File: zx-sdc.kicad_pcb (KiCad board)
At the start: 2 copper layers, 80 x 125.7 mm, 67 parts, among them J1 SD_Card, J2 Micro_SD_Card_Det2, J4 Conn_01x03_Pin, Q1 2N7000, Q2 BC557, U10 74LS125, U11 74LS595, U12 74LS30, U13 74LS138, U3 AMS1117-3.3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

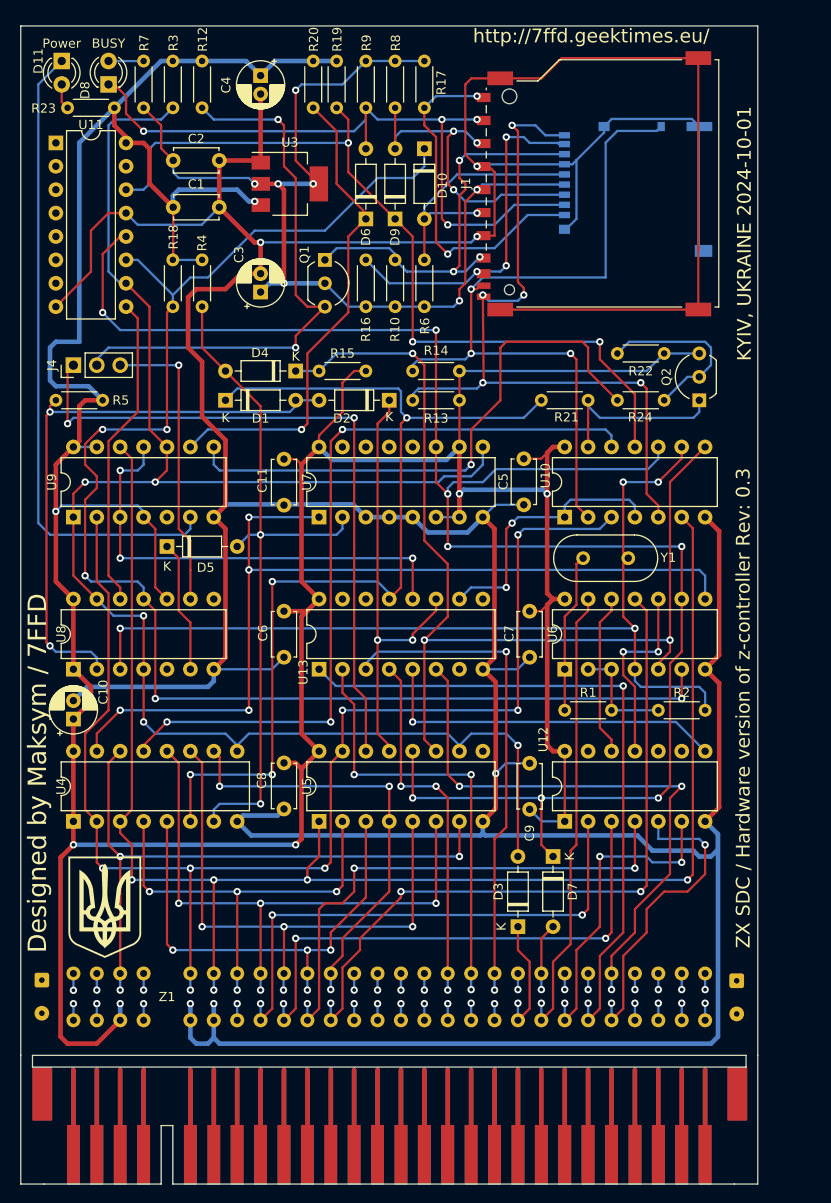
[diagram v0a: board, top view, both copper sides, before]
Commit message: fixed and annotated SD/TEST jumpers
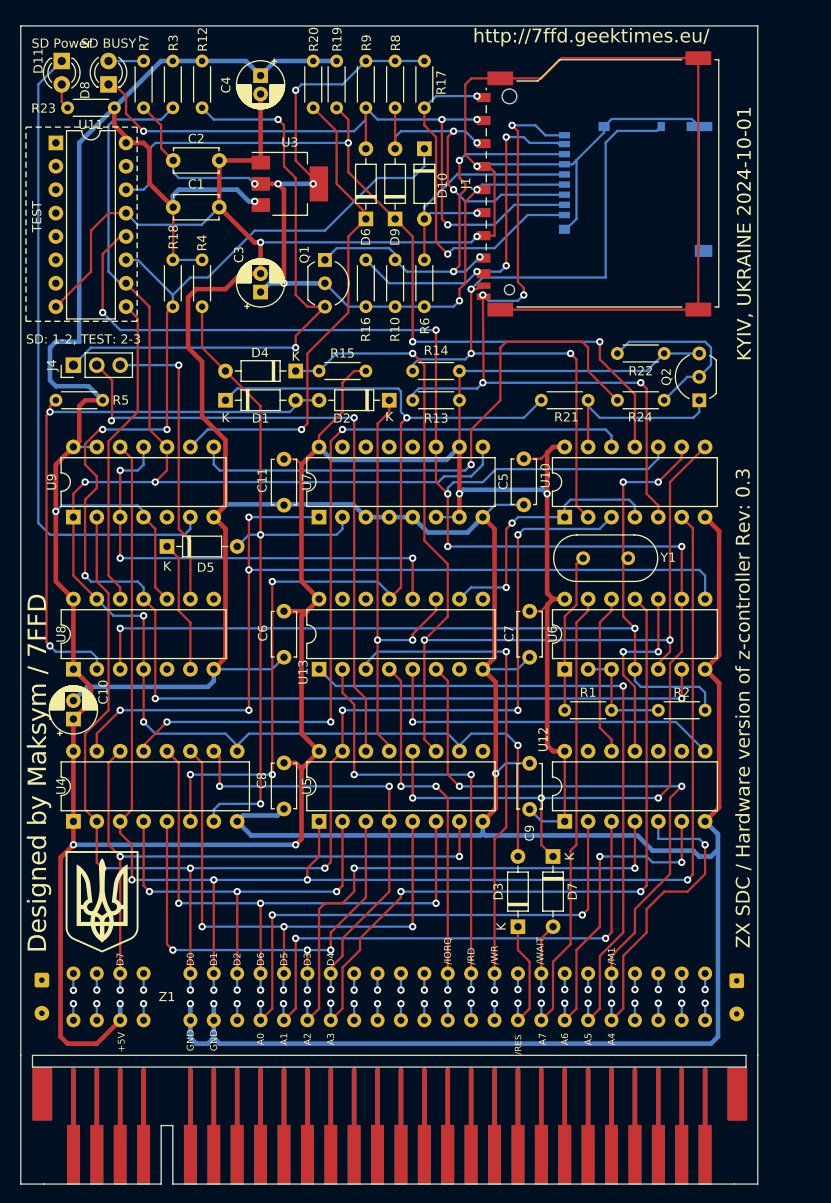
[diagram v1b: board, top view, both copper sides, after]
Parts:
- D11: value Power -> SD Power
- D8: value BUSY -> SD BUSY
- moved UA CoA 0.66 mm to (72.2, 128.4)
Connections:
- J4 pad 1: Net-(J4-Pin_1) -> /SPI_MISO
- J4 pad 2: /SPI_MISO -> Net-(J4-Pin_2)
- U5 pad 14: Net-(J4-Pin_1) -> Net-(J4-Pin_2)
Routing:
- net Net-(J4-Pin_1): track 74.7 -> 0.00 mm, vias 2 -> 0
- net Net-(J4-Pin_2): track 0.00 -> 70.6 mm, vias 0 -> 2
- net /SPI_MISO: track 60.8 -> 63.0 mm
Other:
- board text added: "+5V"
- board text added: "/IORQ"
- board text added: "/M1"
- board text added: "/RD"
- board text added: "/RES"
- board text added: "/WAIT"
- board text added: "/WR"
- board text added: "A0"
- board text added: "A1"
- board text added: "A2"
- board text added: "A3"
- board text added: "A4"
- board text added: "A5"
- board text added: "A6"
- board text added: "A7"
- board text added: "D0"
- board text added: "D1"
- board text added: "D2"
- board text added: "D3"
- board text added: "D4"
- board text added: "D5"
- board text added: "D6"
- board text added: "D7"
- board text added: "GND"
- board text added: "SD: 1-2, TEST: 2-3"
- board text added: "TEST"

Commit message: moved microsd slot close to edge
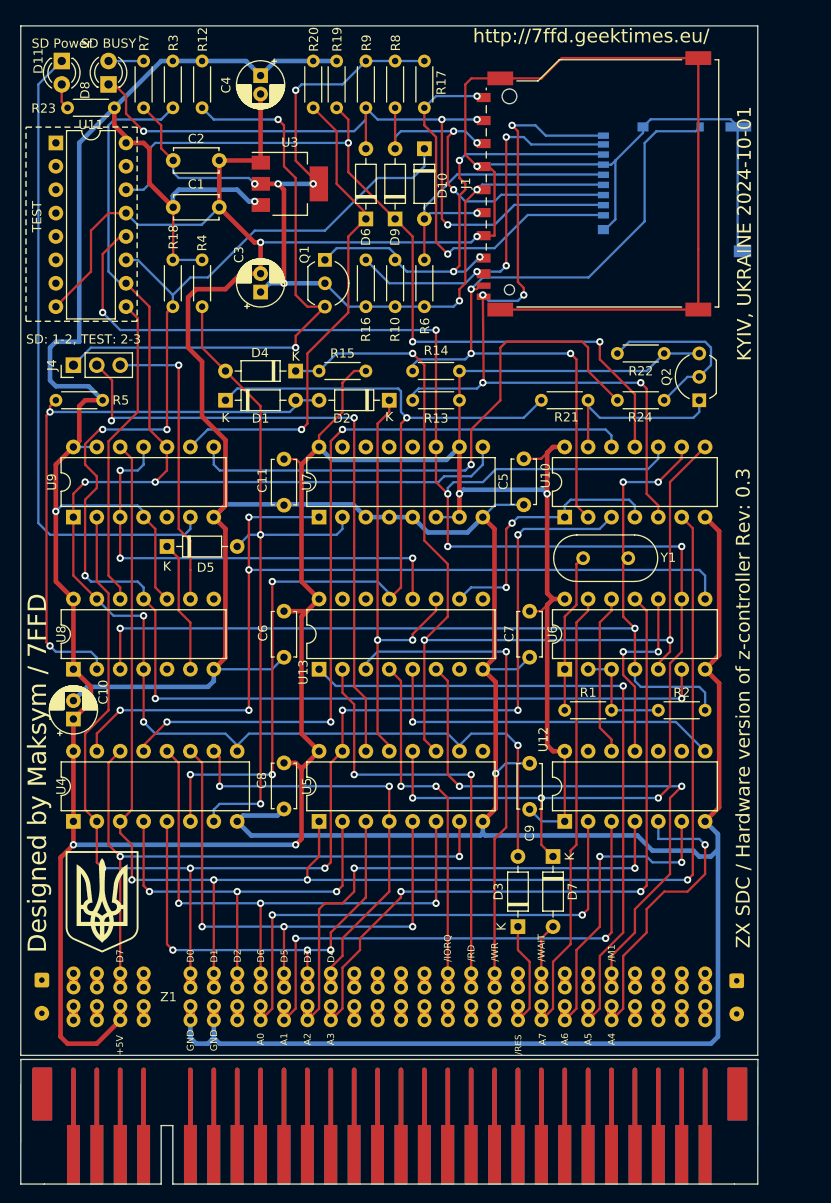
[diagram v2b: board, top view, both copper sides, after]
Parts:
- moved Z1 37.7 mm to (104.7, 141.0), turned to 0 degrees
- moved J2 4.23 mm to (134.4, 57.2)
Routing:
- net Net-(J1-DAT1): track 37.7 -> 41.9 mm
- net Net-(J1-WRITE_PROTECT): track 81.1 -> 85.4 mm
- net Net-(J1-DAT2): track 37.6 -> 41.8 mm
- net Net-(D6-A): track 75.9 -> 80.1 mm
- net Net-(J1-DAT0): track 44.0 -> 48.2 mm
- net Net-(D9-A): track 35.1 -> 39.4 mm
- net Net-(D10-A): track 28.4 -> 32.6 mm
- net +3.3V: track 107.3 -> 111.5 mm
- net unconnected-(Z1-A15-PadA1): track 1.85 -> 0.00 mm, vias 1 -> 0
- net unconnected-(Z1-~{NMI}-PadA14): track 1.83 -> 0.00 mm, vias 1 -> 0
- net unconnected-(Z1-~{MREQ}-PadA16): track 1.83 -> 0.00 mm, vias 1 -> 0
- net unconnected-(Z1-~{INT}-PadA13): track 1.83 -> 0.00 mm, vias 1 -> 0
- net unconnected-(Z1-~{HALT}-PadA15): track 1.83 -> 0.00 mm, vias 1 -> 0
- net unconnected-(Z1-NC-PadA4): track 1.83 -> 0.00 mm, vias 1 -> 0
- net unconnected-(Z1-A13-PadA2): track 1.83 -> 0.00 mm, vias 1 -> 0
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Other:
- outline, holes or cut-outs redrawn
